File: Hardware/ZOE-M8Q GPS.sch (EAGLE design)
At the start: 31 parts, among them J4 U.FL, U1 UBLOX_ZOE_M8-0-10, Y1 32.768kHz

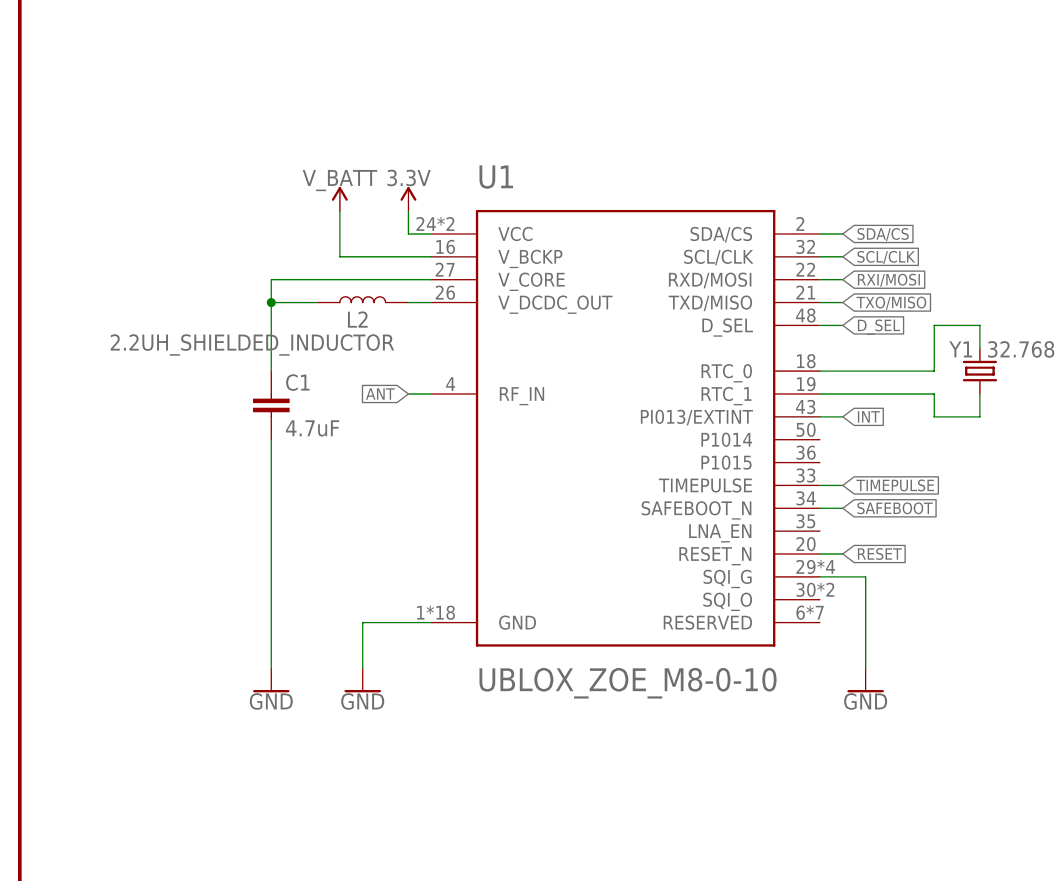
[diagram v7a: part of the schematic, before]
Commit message: Adds more ground vias, ZOE silk to topside, adjusts safteboot trace away from RF in, adds .1uF capactior
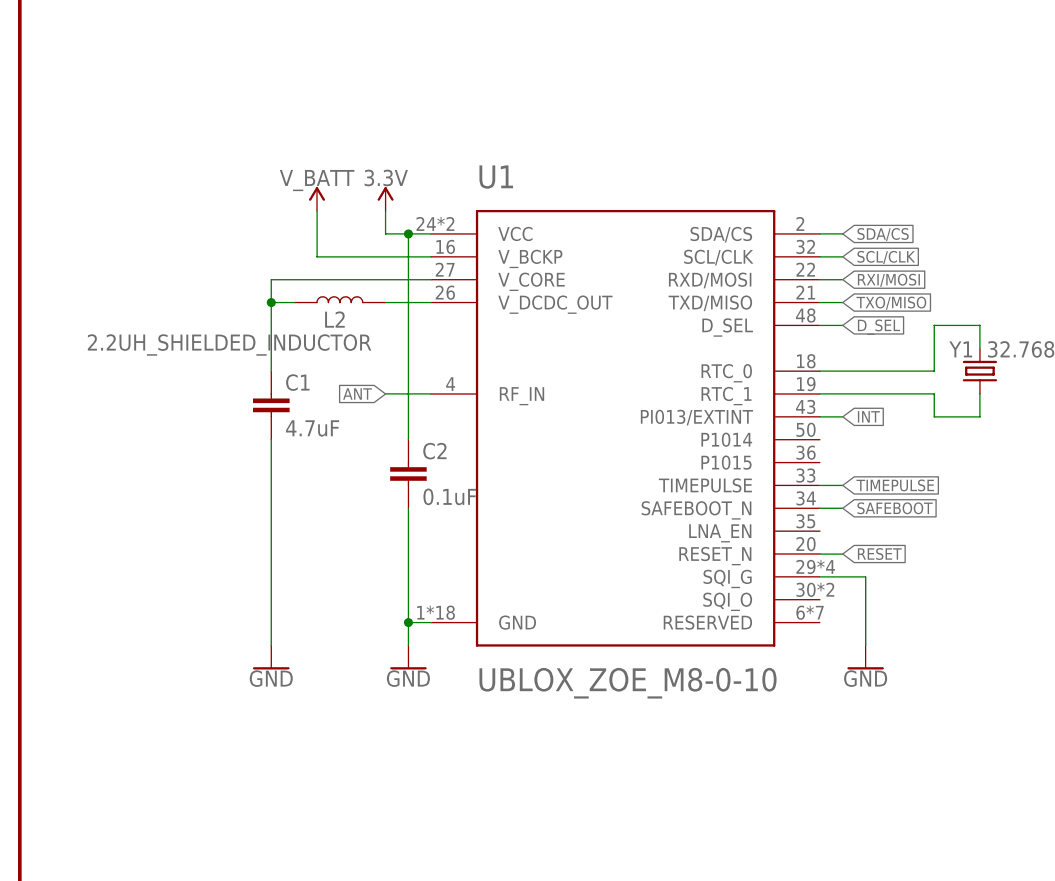
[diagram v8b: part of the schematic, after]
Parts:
- added C2: 0.1uF, SparkFun-Capacitors:0.1UF-0603-25V-(+80/-20%)
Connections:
- net 3.3V: now also C2.1
- net GND: now also C2.2
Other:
- moved on the sheet: L2
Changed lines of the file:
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@@
 <part name="B1" library="SparkFun-Batteries" deviceset="ML414H_IV01E_BATTERY" device=""/>
 <part name="L2" library="SparkFun-Coils" deviceset="2.2UH_SHIELDED_INDUCTOR" device=""/>
+<part name="C2" library="SparkFun-Capacitors" deviceset="0.1UF" device="-0603-25V-(+80/-20%)" value="0.1uF"/>
 </parts>
 <sheets>
@@
 <attribute name="VALUE" x="113.284" y="206.502" size="1.778" layer="96" font="vector" rot="MR0" align="top-center"/>
 </instance>
-<instance part="SUPPLY2" gate="G$1" x="43.18" y="220.98" smashed="yes">
-<attribute name="VALUE" x="43.18" y="223.774" size="1.778" layer="96" align="bottom-center"/>
+<instance part="SUPPLY2" gate="G$1" x="40.64" y="220.98" smashed="yes">
+<attribute name="VALUE" x="40.64" y="223.774" size="1.778" layer="96" align="bottom-center"/>
 </instance>
 <instance part="GND3" gate="1" x="195.58" y="68.58" smashed="yes">
@@
 <attribute name="VALUE" x="386.08" y="244.094" size="1.778" layer="96" align="bottom-center"/>
 </instance>
-<instance part="GND8" gate="1" x="38.1" y="167.64" smashed="yes">
-<attribute name="VALUE" x="38.1" y="167.386" size="1.778" layer="96" align="top-center"/>
-</instance>
-<instance part="GND1" gate="1" x="27.94" y="167.64" smashed="yes">
-<attribute name="VALUE" x="27.94" y="167.386" size="1.778" layer="96" align="top-center"/>
-</instance>
-<instance part="SUPPLY6" gate="G$1" x="35.56" y="220.98" smashed="yes">
-<attribute name="VALUE" x="35.56" y="223.774" size="1.778" layer="96" align="bottom-center"/>
-</instance>
-<instance part="GND9" gate="1" x="93.98" y="167.64" smashed="yes">
-<attribute name="VALUE" x="93.98" y="167.386" size="1.778" layer="96" align="top-center"/>
+<instance part="GND8" gate="1" x="43.18" y="170.18" smashed="yes">
+<attribute name="VALUE" x="43.18" y="169.926" size="1.778" layer="96" align="top-center"/>
+</instance>
+<instance part="GND1" gate="1" x="27.94" y="170.18" smashed="yes">
+<attribute name="VALUE" x="27.94" y="169.926" size="1.778" layer="96" align="top-center"/>
+</instance>
+<instance part="SUPPLY6" gate="G$1" x="33.02" y="220.98" smashed="yes">
+<attribute name="VALUE" x="33.02" y="223.774" size="1.778" layer="96" align="bottom-center"/>
+</instance>
+<instance part="GND9" gate="1" x="93.98" y="170.18" smashed="yes">
+<attribute name="VALUE" x="93.98" y="169.926" size="1.778" layer="96" align="top-center"/>
 </instance>
 <instance part="GND10" gate="1" x="60.96" y="35.56" smashed="yes">
@@
 <attribute name="VALUE" x="76.2" y="46.482" size="1.778" layer="96" font="vector" align="top-center"/>
 </instance>
-<instance part="L2" gate="G$1" x="38.1" y="210.82" smashed="yes" rot="R90">
-<attribute name="NAME" x="38.862" y="209.804" size="1.778" layer="95" font="vector" rot="R180"/>
-<attribute name="VALUE" x="41.656" y="205.486" size="1.778" layer="96" font="vector" rot="R180" align="top-left"/>
+<instance part="L2" gate="G$1" x="35.56" y="210.82" smashed="yes" rot="R90">
+<attribute name="NAME" x="36.322" y="209.804" size="1.778" layer="95" font="vector" rot="R180"/>
+<attribute name="VALUE" x="39.116" y="205.486" size="1.778" layer="96" font="vector" rot="R180" align="top-left"/>
+</instance>
+<instance part="C2" gate="G$1" x="43.18" y="190.5" smashed="yes">
+<attribute name="NAME" x="44.704" y="193.421" size="1.778" layer="95" font="vector"/>
+<attribute name="VALUE" x="44.704" y="188.341" size="1.778" layer="96" font="vector"/>
 </instance>
 </instances>
@@
 <pinref part="U1" gate="G$1" pin="GND"/>
 <pinref part="GND8" gate="1" pin="GND"/>
-<wire x1="45.72" y1="175.26" x2="38.1" y2="175.26" width="0.1524" layer="91"/>
-<wire x1="38.1" y1="175.26" x2="38.1" y2="170.18" width="0.1524" layer="91"/>
+<wire x1="45.72" y1="175.26" x2="43.18" y2="175.26" width="0.1524" layer="91"/>
+<wire x1="43.18" y1="175.26" x2="43.18" y2="172.72" width="0.1524" layer="91"/>
+<pinref part="C2" gate="G$1" pin="2"/>
+<wire x1="43.18" y1="187.96" x2="43.18" y2="175.26" width="0.1524" layer="91"/>
+<junction x="43.18" y="175.26"/>
 </segment>
 <segment>
 <pinref part="C1" gate="G$1" pin="2"/>
 <pinref part="GND1" gate="1" pin="GND"/>
-<wire x1="27.94" y1="195.58" x2="27.94" y2="170.18" width="0.1524" layer="91"/>
+<wire x1="27.94" y1="195.58" x2="27.94" y2="172.72" width="0.1524" layer="91"/>
 </segment>
 <segment>
@@
 <pinref part="GND9" gate="1" pin="GND"/>
 <wire x1="88.9" y1="180.34" x2="93.98" y2="180.34" width="0.1524" layer="91"/>
-<wire x1="93.98" y1="180.34" x2="93.98" y2="170.18" width="0.1524" layer="91"/>
+<wire x1="93.98" y1="180.34" x2="93.98" y2="172.72" width="0.1524" layer="91"/>
 </segment>
 <segment>
@@
 <wire x1="45.72" y1="218.44" x2="43.18" y2="218.44" width="0.1524" layer="91"/>
 <pinref part="SUPPLY2" gate="G$1" pin="3.3V"/>
-<wire x1="43.18" y1="220.98" x2="43.18" y2="218.44" width="0.1524" layer="91"/>
+<wire x1="43.18" y1="218.44" x2="40.64" y2="218.44" width="0.1524" layer="91"/>
+<wire x1="40.64" y1="220.98" x2="40.64" y2="218.44" width="0.1524" layer="91"/>
+<pinref part="C2" gate="G$1" pin="1"/>
+<wire x1="43.18" y1="218.44" x2="43.18" y2="195.58" width="0.1524" layer="91"/>
+<junction x="43.18" y="218.44"/>
 </segment>
 <segment>
@@
 <segment>
 <pinref part="U1" gate="G$1" pin="V_DCDC_OUT"/>
-<wire x1="45.72" y1="210.82" x2="43.18" y2="210.82" width="0.1524" layer="91"/>
+<wire x1="45.72" y1="210.82" x2="40.64" y2="210.82" width="0.1524" layer="91"/>
 <pinref part="L2" gate="G$1" pin="2"/>
 </segment>
@@
 <net name="N$6" class="0">
 <segment>
-<wire x1="33.02" y1="210.82" x2="27.94" y2="210.82" width="0.1524" layer="91"/>
+<wire x1="30.48" y1="210.82" x2="27.94" y2="210.82" width="0.1524" layer="91"/>
 <wire x1="27.94" y1="210.82" x2="27.94" y2="213.36" width="0.1524" layer="91"/>
 <pinref part="U1" gate="G$1" pin="V_CORE"/>
@@
 <pinref part="U1" gate="G$1" pin="V_BCKP"/>
 <pinref part="SUPPLY6" gate="G$1" pin="V_BATT"/>
-<wire x1="45.72" y1="215.9" x2="35.56" y2="215.9" width="0.1524" layer="91"/>
-<wire x1="35.56" y1="215.9" x2="35.56" y2="220.98" width="0.1524" layer="91"/>
+<wire x1="45.72" y1="215.9" x2="33.02" y2="215.9" width="0.1524" layer="91"/>
+<wire x1="33.02" y1="215.9" x2="33.02" y2="220.98" width="0.1524" layer="91"/>
 </segment>
 <segment>
@@
 <segment>
 <pinref part="U1" gate="G$1" pin="RF_IN"/>
-<wire x1="45.72" y1="200.66" x2="43.18" y2="200.66" width="0.1524" layer="91"/>
-<label x="43.18" y="200.66" size="1.27" layer="95" rot="R180" xref="yes"/>
-</segment>
-<segment>
+<wire x1="45.72" y1="200.66" x2="40.64" y2="200.66" width="0.1524" layer="91"/>
+<label x="40.64" y="200.66" size="1.27" layer="95" rot="R180" xref="yes"/>
+</segment>
+<segment>
